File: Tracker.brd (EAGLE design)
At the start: 57.1 x 68.2 mm, 37 parts, among them IC2 74AHC1G125DBV, IC3 74AHC1G125DBV, M1 HX1, X1 BU-SMA-V

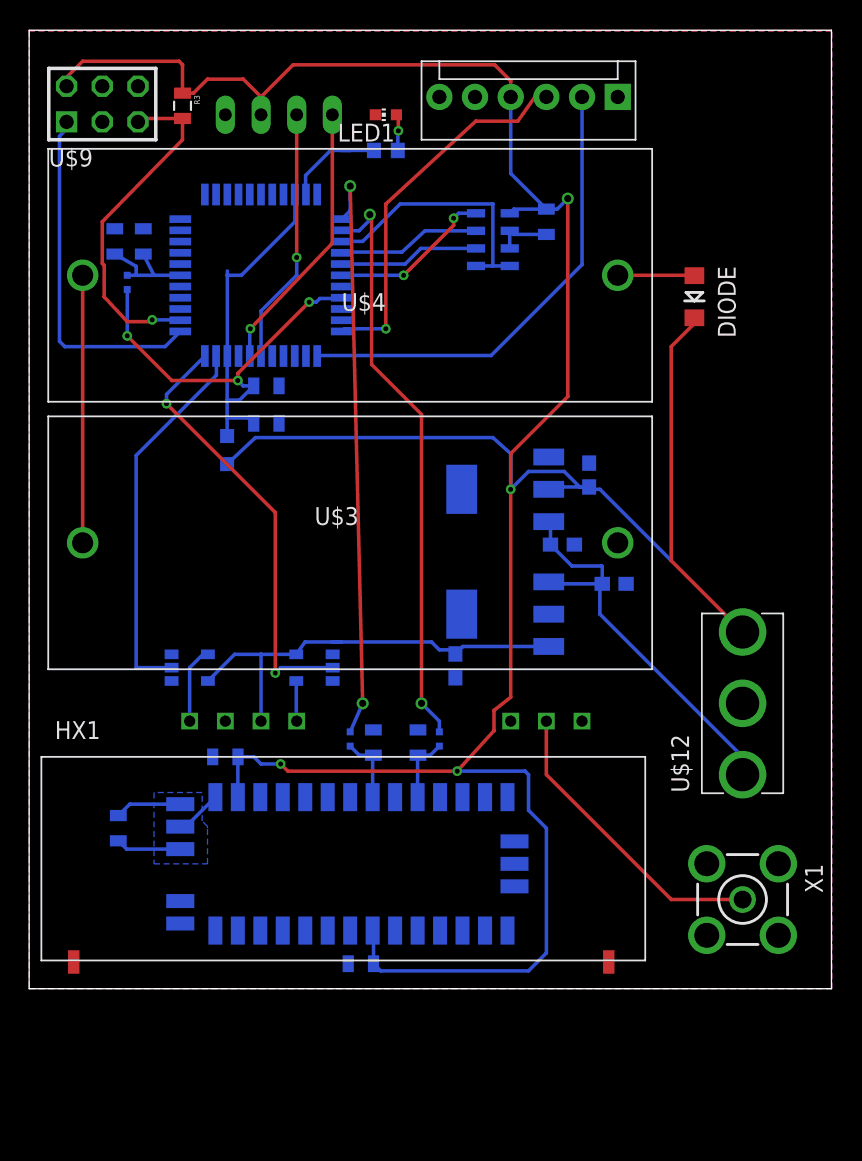
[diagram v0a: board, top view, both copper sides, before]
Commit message: rev2
Removed .x#h files, removed teaching examples, shrunk footprint, made project library
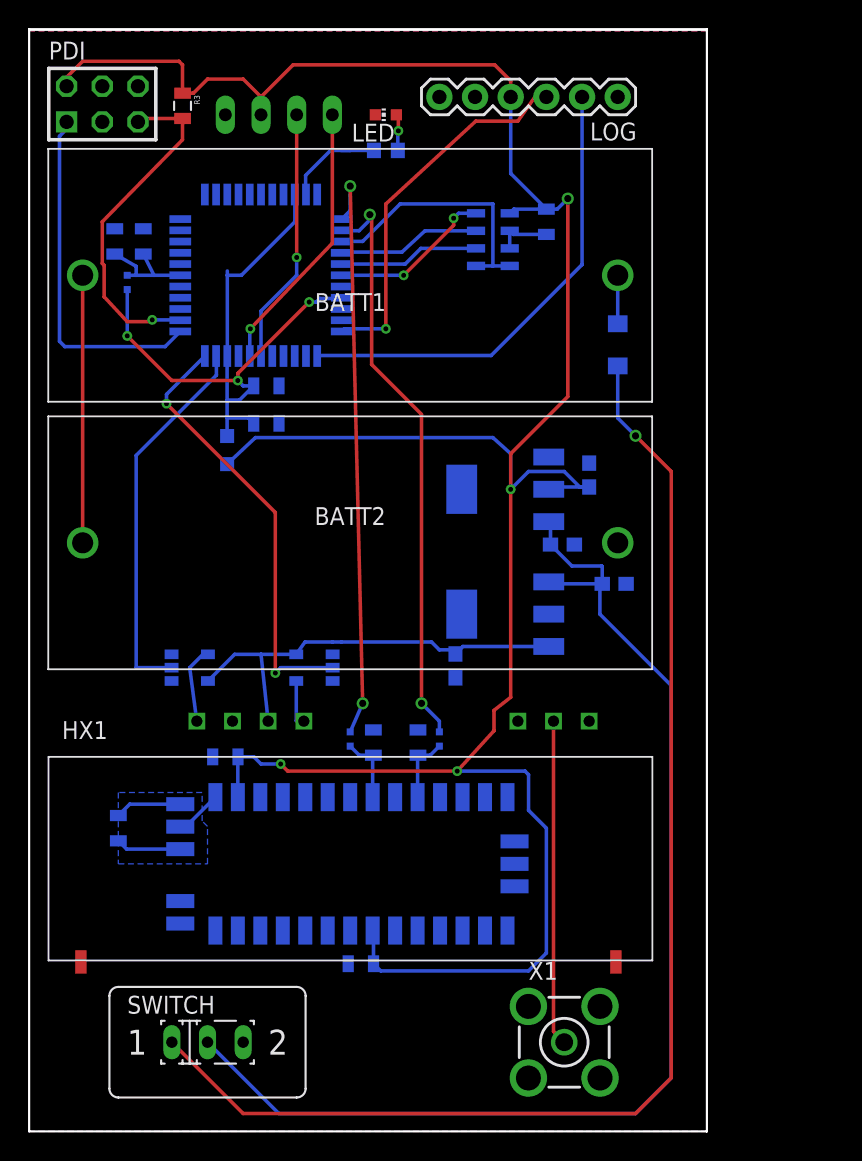
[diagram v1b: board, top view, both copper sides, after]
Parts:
- removed JP4: (no value), SparkFun:MOLEX-1X6
- removed U$12: CKN10160-ND, SHC:ZMCHFL3R
- removed U$9: AVR-PDIVERT, avr-7:AVR-ISP-6
- added LOG: LOG, Tracker:SPARKFUN_1X06
- added PDI: AVR-7_AVR-PDIVERT, Tracker:AVR-7_AVR-ISP-6
- added SWITCH: (no value), switch:M251
- L1: value 10uH -> FB_0402; device rcl:L2012C -> rc-master-smd:L0402
- L3: value FB_0402 -> 10uH; device rc-master-smd:L0402 -> rcl:L2012C
- moved L2 39.4 mm to (29.2, 17.8)
- moved L4 39.4 mm to (6.99, 50.3)
- moved L1 22.4 mm to (22.9, 17.8)
- moved L3 22.4 mm to (14.1, 38.4)
- moved X1 16.3 mm to (38.1, -3.81), turned to 0 degrees
- moved DIODE 6.45 mm to (41.9, 45.8), flipped to the bottom
- moved M1 0.51 mm to (39.9, 10.2)
- renumbered IC1 to MCU, IC2 to LOG1, IC3 to LOG2, LED1 to LED, U$1 to MS5607, U$10 to 3.3REG, U$11 to 5.0REG, U$2 to GPS, U$3 to BATT2, U$4 to BATT1
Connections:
- removed net N$11: DIODE.C, U$12.3
- removed net N$17: C15.2, C16.2, L2.1, MCU.39
- new net AVCC: C15.2, C16.2, L4.1, MCU.39
- new net N$7: DIODE.C, SWITCH.1
- net BATT: now also SWITCH.2; no longer U$12.1
- net GND: now also LOG.5, PDI.6; no longer JP4.5, U$9.6
- net N$1: now also L1.2; no longer L3.2
- net N$18: now also L3.1, L4.2; no longer L1.1, L2.2
- net N$2: now also L2.2; no longer L4.2
- net PDI-CLK: now also PDI.5; no longer U$9.5
- net PDI-DATA: now also PDI.1; no longer U$9.1
- net RXC: now also L1.1; no longer L3.1
- net RXD: now also LOG.3; no longer JP4.3
- net TXC: now also L2.1; no longer L4.1
- net TXD: now also LOG.2; no longer JP4.2
- net VCC: now also L3.2, LOG.4, PDI.2; no longer JP4.4, L1.2, U$9.2
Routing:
- net N$7: track 0.00 -> 91.0 mm, vias 0 -> 1
- net BATT: track 29.2 -> 84.8 mm
- net N$11: track 25.2 -> 0.00 mm
- net VCC: track 191.5 -> 183.5 mm
- net N$17: track 7.86 -> 0.00 mm
- net AVCC: track 0.00 -> 7.86 mm
- net N$6: track 5.47 -> 3.45 mm
- net N$5: track 21.5 -> 23.2 mm
- net 5V: track 31.5 -> 30.9 mm
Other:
- board size 57.1 x 68.2 mm -> 48.3 x 78.5 mm

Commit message: DRILL KILL
added drills, sorry for bad commit summary
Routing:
- net N$7: track 91.0 -> 89.9 mm
- net BATT: track 84.8 -> 83.8 mm
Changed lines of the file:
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@@
 <wire x1="48.26" y1="68.326" x2="0" y2="68.326" width="0.1524" layer="20"/>
 <wire x1="0" y1="68.326" x2="0" y2="-10.16" width="0.1524" layer="20"/>
+<hole x="2.54" y="-7.62" drill="2.4638"/>
+<hole x="2.54" y="20.32" drill="2.4638"/>
+<hole x="45.72" y="64.77" drill="2.4638"/>
+<hole x="45.72" y="-7.62" drill="2.4638"/>
 </plain>
 <attributes>
@@
 </class>
 </classes>
-<designrules name="oshpark-2layer">
+<designrules name="SeeedStudio_2layer_DRU_no_angle_20140221">
 <description language="de">&lt;b&gt;EAGLE Design Rules&lt;/b&gt;
 &lt;p&gt;
@@
 Einstellungen hier und speichern die Design Rules unter
 einem neuen Namen ab.</description>
-<description language="en">&lt;b&gt;Laen's PCB Order Design Rules&lt;/b&gt;
+<description language="en">&lt;b&gt;EAGLE Design Rules&lt;/b&gt;
 &lt;p&gt;
-Please make sure your boards conform to these design rules.</description>
+The default Design Rules have been set to cover
+a wide range of applications. Your particular design
+may have different requirements, so please make the
+necessary adjustments and save your customized
+design rules under a new name.</description>
+<description language="zh">&lt;b&gt;Seeed Studio EAGLE Design Rules&lt;/b&gt;
+</description>
 <param name="layerSetup" value="(1*16)"/>
-<param name="mtCopper" value="0.0356mm 0.0356mm 0.0356mm 0.0356mm 0.0356mm 0.0356mm 0.0356mm 0.0356mm 0.0356mm 0.0356mm 0.0356mm 0.0356mm 0.0356mm 0.0356mm 0.0356mm 0.0356mm"/>
-<param name="mtIsolate" value="1.5011mm 0.1499mm 0.2007mm 0.1499mm 0.2007mm 0.1499mm 0.2007mm 0.1499mm 0.2007mm 0.1499mm 0.2007mm 0.1499mm 0.2007mm 0.1499mm 0.2007mm"/>
+<param name="mtCopper" value="0.035mm 0.0175mm 0.035mm 0.035mm 0.035mm 0.035mm 0.035mm 0.035mm 0.035mm 0.035mm 0.035mm 0.035mm 0.035mm 0.035mm 0.0175mm 0.035mm"/>
+<param name="mtIsolate" value="1.5mm 1.1mm 0.2mm 0.15mm 0.2mm 0.15mm 0.2mm 0.15mm 0.2mm 0.15mm 0.2mm 0.15mm 0.2mm 0.15mm 0.2mm"/>
 <param name="mdWireWire" value="6mil"/>
 <param name="mdWirePad" value="6mil"/>
@@
 <param name="mdPadVia" value="6mil"/>
 <param name="mdViaVia" value="6mil"/>
-<param name="mdSmdPad" value="6mil"/>
-<param name="mdSmdVia" value="6mil"/>
-<param name="mdSmdSmd" value="6mil"/>
+<param name="mdSmdPad" value="0mil"/>
+<param name="mdSmdVia" value="0mil"/>
+<param name="mdSmdSmd" value="0mil"/>
 <param name="mdViaViaSameLayer" value="8mil"/>
 <param name="mnLayersViaInSmd" value="2"/>
-<param name="mdCopperDimension" value="15mil"/>
-<param name="mdDrill" value="6mil"/>
+<param name="mdCopperDimension" value="10mil"/>
+<param name="mdDrill" value="10mil"/>
 <param name="mdSmdStop" value="0mil"/>
 <param name="msWidth" value="6mil"/>
-<param name="msDrill" value="13mil"/>
-<param name="msMicroVia" value="13mil"/>
+<param name="msDrill" value="12mil"/>
+<param name="msMicroVia" value="12mil"/>
 <param name="msBlindViaRatio" value="0.5"/>
 <param name="rvPadTop" value="0.25"/>
@@
 <param name="rvMicroViaOuter" value="0.25"/>
 <param name="rvMicroViaInner" value="0.25"/>
-<param name="rlMinPadTop" value="7mil"/>
+<param name="rlMinPadTop" value="10mil"/>
 <param name="rlMaxPadTop" value="20mil"/>
-<param name="rlMinPadInner" value="7mil"/>
+<param name="rlMinPadInner" value="10mil"/>
 <param name="rlMaxPadInner" value="20mil"/>
-<param name="rlMinPadBottom" value="7mil"/>
+<param name="rlMinPadBottom" value="10mil"/>
 <param name="rlMaxPadBottom" value="20mil"/>
-<param name="rlMinViaOuter" value="7mil"/>
+<param name="rlMinViaOuter" value="6mil"/>
 <param name="rlMaxViaOuter" value="20mil"/>
-<param name="rlMinViaInner" value="7mil"/>
+<param name="rlMinViaInner" value="6mil"/>
 <param name="rlMaxViaInner" value="20mil"/>
 <param name="rlMinMicroViaOuter" value="4mil"/>
@@
 <param name="psTop" value="-1"/>
 <param name="psBottom" value="-1"/>
-<param name="psFirst" value="-1"/>
+<param name="psFirst" value="0"/>
 <param name="psElongationLong" value="100"/>
 <param name="psElongationOffset" value="100"/>
 <param name="mvStopFrame" value="1"/>
 <param name="mvCreamFrame" value="0"/>
-<param name="mlMinStopFrame" value="2.5mil"/>
-<param name="mlMaxStopFrame" value="2.5mil"/>
+<param name="mlMinStopFrame" value="2mil"/>
+<param name="mlMaxStopFrame" value="2mil"/>
 <param name="mlMinCreamFrame" value="0mil"/>
 <param name="mlMaxCreamFrame" value="0mil"/>
-<param name="mlViaStopLimit" value="0mil"/>
+<param name="mlViaStopLimit" value="100mil"/>
 <param name="srRoundness" value="0"/>
 <param name="srMinRoundness" value="0mil"/>
@@
 <param name="checkAngle" value="0"/>
 <param name="checkFont" value="1"/>
-<param name="checkRestrict" value="1"/>
+<param name="checkRestrict" value="0"/>
 <param name="useDiameter" value="13"/>
 <param name="maxErrors" value="50"/>
@@
 <wire x1="40.806" y1="30.06" x2="40.767" y2="30.099" width="0.254" layer="16"/>
 <wire x1="40.767" y1="30.099" x2="38.647" y2="30.099" width="0.254" layer="16"/>
-<wire x1="45.72" y1="-6.35" x2="43.18" y2="-8.89" width="0.254" layer="16"/>
-<wire x1="45.72" y1="-6.35" x2="45.72" y2="21.59" width="0.254" layer="16"/>
+<wire x1="45.72" y1="-4.572" x2="41.402" y2="-8.89" width="0.254" layer="16"/>
+<wire x1="45.72" y1="-4.572" x2="45.72" y2="21.59" width="0.254" layer="16"/>
 <wire x1="45.72" y1="21.59" x2="40.64" y2="26.67" width="0.254" layer="16"/>
 <contactref element="SWITCH" pad="2"/>
 <wire x1="17.78" y1="-8.89" x2="12.7" y2="-3.81" width="0.254" layer="16"/>
-<wire x1="43.18" y1="-8.89" x2="17.78" y2="-8.89" width="0.254" layer="16"/>
+<wire x1="41.402" y1="-8.89" x2="17.78" y2="-8.89" width="0.254" layer="16"/>
 </signal>
 <signal name="N$4">
@@
 <via x="43.18" y="39.37" extent="1-16" drill="0.508"/>
 <wire x1="43.18" y1="39.37" x2="45.72" y2="36.83" width="0.254" layer="1"/>
-<wire x1="45.72" y1="36.83" x2="45.72" y2="-6.35" width="0.254" layer="1"/>
-<wire x1="45.72" y1="-6.35" x2="43.18" y2="-8.89" width="0.254" layer="1"/>
-<wire x1="43.18" y1="-8.89" x2="15.24" y2="-8.89" width="0.254" layer="1"/>
+<wire x1="45.72" y1="36.83" x2="45.72" y2="-4.572" width="0.254" layer="1"/>
+<wire x1="45.72" y1="-4.572" x2="41.402" y2="-8.89" width="0.254" layer="1"/>
+<wire x1="41.402" y1="-8.89" x2="15.24" y2="-8.89" width="0.254" layer="1"/>
 <wire x1="15.24" y1="-8.89" x2="10.16" y2="-3.81" width="0.254" layer="1"/>
 </signal>
